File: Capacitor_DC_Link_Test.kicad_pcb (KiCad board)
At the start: 2 copper layers, 67.7 x 66.6 mm, 10 parts, among them J1 Conn_01x02, J2 Conn_01x02, J3 Conn_01x02, J4 Conn_01x02, J5 Conn_01x02, J6 Conn_01x02

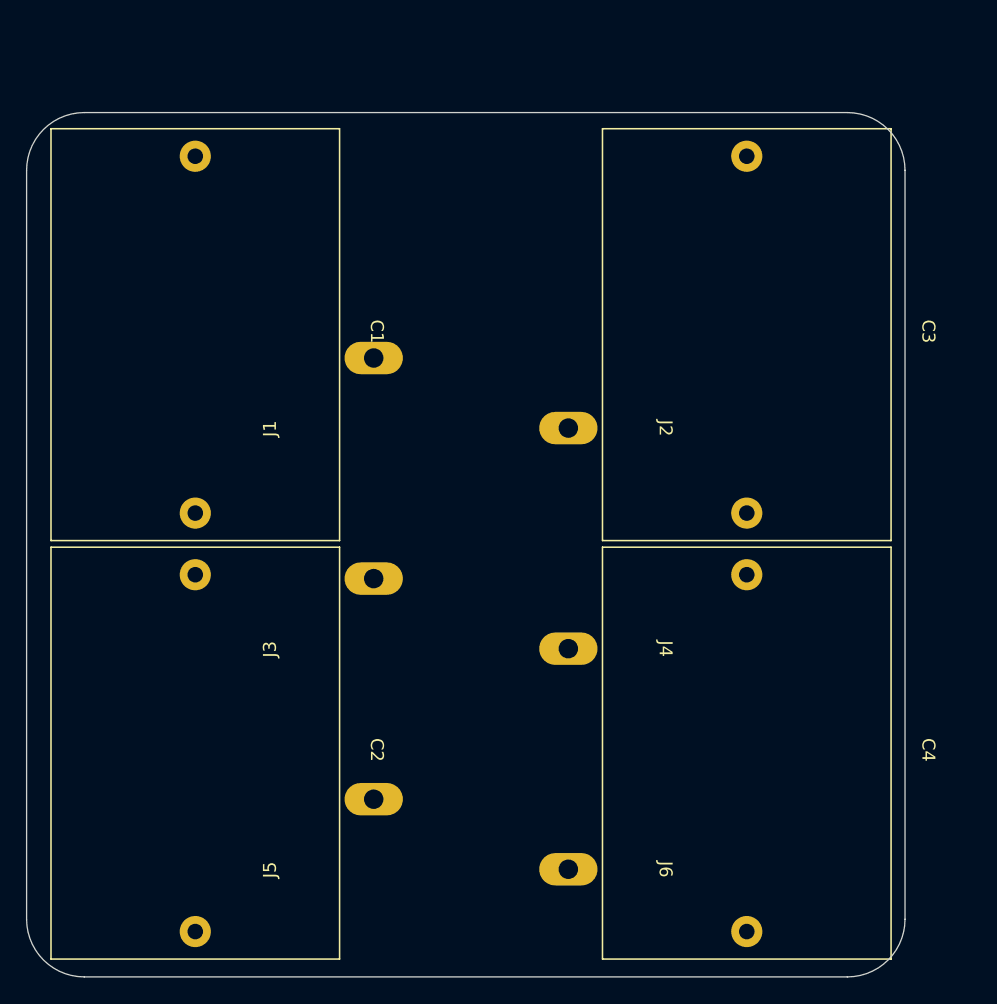
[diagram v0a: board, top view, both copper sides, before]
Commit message: VER1.0: добавил модели конденсаторов
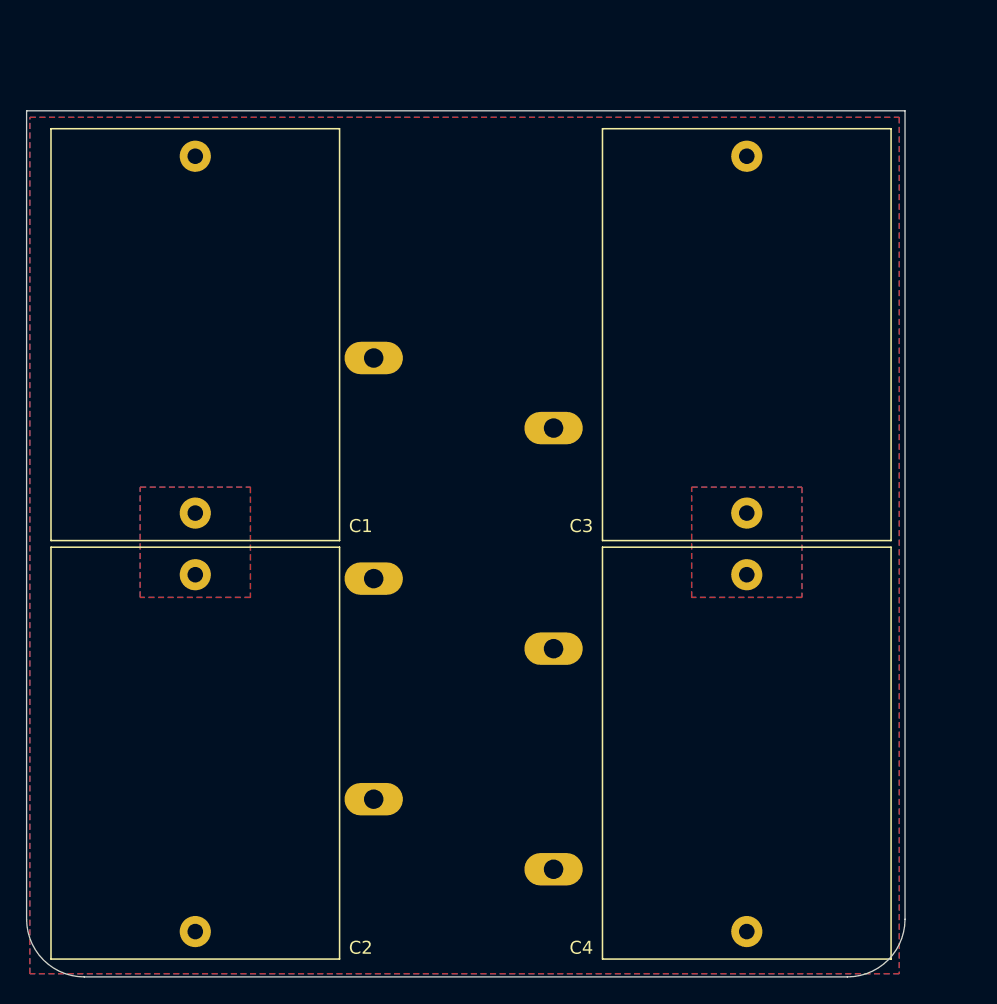
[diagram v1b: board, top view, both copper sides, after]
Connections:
- C1 pad 1: Net-(C1-Pad1) -> VDD
- C2 pad 2: Net-(C2-Pad2) -> GNDPWR
- C3 pad 1: Net-(C1-Pad1) -> VDD
- C4 pad 2: Net-(C2-Pad2) -> GNDPWR
- J1 pad 1: unconnected-(J1-Pin_1-Pad1) -> GNDPWR
- J2 pad 1: unconnected-(J2-Pin_1-Pad1) -> VDD
- J3 pad 1: unconnected-(J3-Pin_1-Pad1) -> GNDPWR
- J4 pad 1: unconnected-(J4-Pin_1-Pad1) -> VDD
- J5 pad 1: unconnected-(J5-Pin_1-Pad1) -> GNDPWR
- J6 pad 1: unconnected-(J6-Pin_1-Pad1) -> VDD
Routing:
- added copper zone on B.Cu, net GNDPWR
- added copper zone on B.Cu, net Net-(C1-Pad2)
- added copper zone on F.Cu, net Net-(C1-Pad2)
- added copper zone on B.Cu, net Net-(C3-Pad2)
- added copper zone on F.Cu, net Net-(C3-Pad2)
- added copper zone on F.Cu, net VDD
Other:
- board size 67.7 x 66.6 mm -> 67.7 x 66.7 mm

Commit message: VER1.0: расширил плату
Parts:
- added J7: Conn_01x02, Bush_My:Low_IN, F.Cu at (139.0, 59.5)
- added J8: Conn_01x02, Bush_My:High_IN, F.Cu at (166.0, 59.5)
- moved J2 5.00 mm to (166.0, 76.5)
- moved J4 5.00 mm to (166.0, 93.5)
- moved J6 5.00 mm to (166.0, 110.5)
- moved C3 4.00 mm to (171.8, 55.5)
- moved C4 4.00 mm to (171.8, 87.8)
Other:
- board size 67.7 x 66.7 mm -> 72.7 x 67.8 mm
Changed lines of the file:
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@@
 	(footprint "Bush_My:High_IN"
 		(layer "F.Cu")
-		(at 161 110.45 -90)
+		(at 166 110.45 -90)
 		(property "Reference" "J6"
 			(at 0 -0.5 270)
@@
 		(embedded_fonts no)
 	)
+	(footprint "Bush_My:High_IN"
+		(layer "F.Cu")
+		(at 166 59.45 -90)
+		(property "Reference" "J8"
+			(at 0 -0.5 270)
+			(unlocked yes)
+			(layer "F.SilkS")
+			(hide yes)
+			(effects
+				(font
+					(size 1 1)
+					(thickness 0.1)
+				)
+			)
+		)
+		(property "Value" "Conn_01x02"
+			(at 0 1 270)
+			(unlocked yes)
+			(layer "F.Fab")
+			(effects
+				(font
+					(size 1 1)
+					(thickness 0.15)
+				)
+			)
+		)
+		(property "Datasheet" "~"
+			(at 0 0 270)
+			(unlocked yes)
+			(layer "F.Fab")
+			(hide yes)
+			(effects
+				(font
+					(size 1 1)
+					(thickness 0.15)
+				)
+			)
+		)
+		(property "Description" "Generic connector, single row, 01x02, script generated (kicad-library-utils/schlib/autogen/connector/)"
+			(at 0 0 270)
+			(unlocked yes)
+			(layer "F.Fab")
+			(hide yes)
+			(effects
+				(font
+					(size 1 1)
+					(thickness 0.15)
+				)
+			)
+		)
+		(property ki_fp_filters "Connector*:*_1x??_*")
+		(sheetname "/")
+		(sheetfile "Capacitor_DC_Link_Test.kicad_sch")
+		(attr smd)
+		(fp_text user "${REFERENCE}"
+			(at 0 2.5 270)
+			(unlocked yes)
+			(layer "F.Fab")
+			(effects
+				(font
+					(size 1 1)
+					(thickness 0.15)
+				)
+			)
+		)
+		(pad "1" thru_hole oval
+			(at 0 8.14 270)
+			(size 2.5 4.5)
+			(drill 1.5)
+			(layers "*.Cu" "*.Mask")
+			(remove_unused_layers no)
+			(net 2 "VDD")
+			(pinfunction "Pin_1")
+			(pintype "passive")
+			(clearance 2.5)
+		)
+		(embedded_fonts no)
+	)
 	(footprint "Bush_My:Low_IN"
 		(layer "F.Cu")
@@
 	(footprint "Capacitor_my:Capacitor_22x36.5x31.5"
 		(layer "F.Cu")
-		(at 167.75 55.5 -90)
+		(at 171.75 55.5 -90)
 		(property "Reference" "C3"
 			(at 28.5 12.75 0)
@@
 	(footprint "Bush_My:High_IN"
 		(layer "F.Cu")
-		(at 161 93.45 -90)
+		(at 166 93.45 -90)
 		(property "Reference" "J4"
 			(at 0 -0.5 270)
@@
 	(footprint "Bush_My:High_IN"
 		(layer "F.Cu")
-		(at 161 76.45 -90)
+		(at 166 76.45 -90)
 		(property "Reference" "J2"
 			(at 0 -0.5 270)
@@
 		)
 	)
+	(footprint "Bush_My:Low_IN"
+		(layer "F.Cu")
+		(at 139 59.5 90)
+		(property "Reference" "J7"
+			(at 0 -8 90)
+			(unlocked yes)
+			(layer "F.SilkS")
+			(hide yes)
+			(effects
+				(font
+					(size 1 1)
+					(thickness 0.1)
+				)
+			)
+		)
+		(property "Value" "Conn_01x02"
+			(at 0 -6.5 90)
+			(unlocked yes)
+			(layer "F.Fab")
+			(effects
+				(font
+					(size 1 1)
+					(thickness 0.15)
+				)
+			)
+		)
+		(property "Datasheet" "~"
+			(at 0 0 90)
+			(unlocked yes)
+			(layer "F.Fab")
+			(hide yes)
+			(effects
+				(font
+					(size 1 1)
+					(thickness 0.15)
+				)
+			)
+		)
+		(property "Description" "Generic connector, single row, 01x02, script generated (kicad-library-utils/schlib/autogen/connector/)"
+			(at 0 0 90)
+			(unlocked yes)
+			(layer "F.Fab")
+			(hide yes)
+			(effects
+				(font
+					(size 1 1)
+					(thickness 0.15)
+				)
+			)
+		)
+		(property ki_fp_filters "Connector*:*_1x??_*")
+		(sheetname "/")
+		(sheetfile "Capacitor_DC_Link_Test.kicad_sch")
+		(attr smd)
+		(fp_text user "${REFERENCE}"
+			(at 0 -5 90)
+			(unlocked yes)
+			(layer "F.Fab")
+			(effects
+				(font
+					(size 1 1)
+					(thickness 0.15)
+				)
+			)
+		)
+		(pad "1" thru_hole oval
+			(at 5.45 0 90)
+			(size 2.5 4.5)
+			(drill 1.5)
+			(layers "*.Cu" "*.Mask")
+			(remove_unused_layers no)
+			(net 1 "GNDPWR")
+			(pinfunction "Pin_1")
+			(pintype "passive")
+			(clearance 2.5)
+		)
+		(embedded_fonts no)
+	)
 	(footprint "Capacitor_my:Capacitor_22x36.5x31.5"
 		(layer "F.Cu")
-		(at 167.75 87.75 -90)
+		(at 171.75 87.75 -90)
 		(property "Reference" "C4"
 			(at 28.75 12.75 0)
@@
 	)
 	(gr_line
-		(start 179.944999 114.3)
-		(end 179.944999 52)
+		(start 184.944999 114.3)
+		(end 184.945 50.995)
 		(stroke
 			(width 0.1)
@@
 	)
 	(gr_line
-		(start 112.25 52)
+		(start 112.25 50.995)
 		(end 112.25 114.3)
 		(stroke
@@
 	)
 	(gr_line
-		(start 179.944999 52)
-		(end 112.25 52)
+		(start 184.945 50.995)
+		(end 112.25 51)
 		(stroke
 			(width 0.1)
@@
 	)
 	(gr_arc
-		(start 179.944999 114.3)
-		(mid 178.643089 117.443089)
-		(end 175.499999 118.745)
+		(start 184.944999 114.3)
+		(mid 183.643089 117.443089)
+		(end 180.499999 118.745)
 		(stroke
 			(width 0.1)
@@
 	)
 	(gr_line
-		(start 175.499999 118.745)
+		(start 180.5 118.745)
 		(end 116.695 118.745)
 		(stroke
@@
 		(polygon
 			(pts
-				(xy 112.5 52.5) (xy 179.5 52.5) (xy 179.5 118.5) (xy 112.5 118.5)
+				(xy 112.5 51) (xy 184.75 51) (xy 184.75 118.5) (xy 112.5 118.5)
 			)
 		)
@@
 		(polygon
 			(pts
-				(xy 163.5 81) (xy 172 81) (xy 172 89.5) (xy 163.5 89.5)
+				(xy 167.5 81) (xy 176 81) (xy 176 89.5) (xy 167.5 89.5)
 			)
 		)
@@
 		(polygon
 			(pts
-				(xy 112.501876 52.499889) (xy 179.501876 52.499889) (xy 179.501876 118.499889) (xy 112.501876 118.499889)
-			)
-		)
+				(xy 112.501876 50.999889) (xy 184.751876 50.999889) (xy 184.751876 118.499889) (xy 112.501876 118.499889)
+			)
+		)

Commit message: VER1.0: добавил вводные шины
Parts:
- added J10: Conn_01x01, Bush_My:Bush_5x3, F.Cu at (148.2, 112.2)
- added J11: Conn_01x01, Bush_My:Bush_5x3, F.Cu at (148.2, 78.2)
- added J12: Conn_01x01, Bush_My:Bush_5x3, F.Cu at (148.2, 92.2)
- added J9: Conn_01x01, Bush_My:Bush_5x3, F.Cu at (148.2, 58.2)

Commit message: VER1.0: изменил шины
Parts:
- added J13: Conn_01x01, Bush_My:Bush_5x3, F.Cu at (152.9, 110.5)
- added J14: Conn_01x01, Bush_My:Bush_5x3, F.Cu at (143.9, 54.0)
- added J15: Conn_01x01, Bush_My:Bush_5x3, F.Cu at (152.9, 93.5)
- added J16: Conn_01x01, Bush_My:Bush_5x3, F.Cu at (143.9, 71.0)
- moved J10 8.40 mm to (143.9, 105.0)
- moved J12 6.01 mm to (143.9, 88.0)
- moved J11 5.06 mm to (152.9, 76.5)
- moved J9 4.91 mm to (152.9, 59.5)
